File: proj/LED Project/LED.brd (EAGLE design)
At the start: 100 x 80 mm, 3 parts, among them U1 ATMEGA328P-AUR

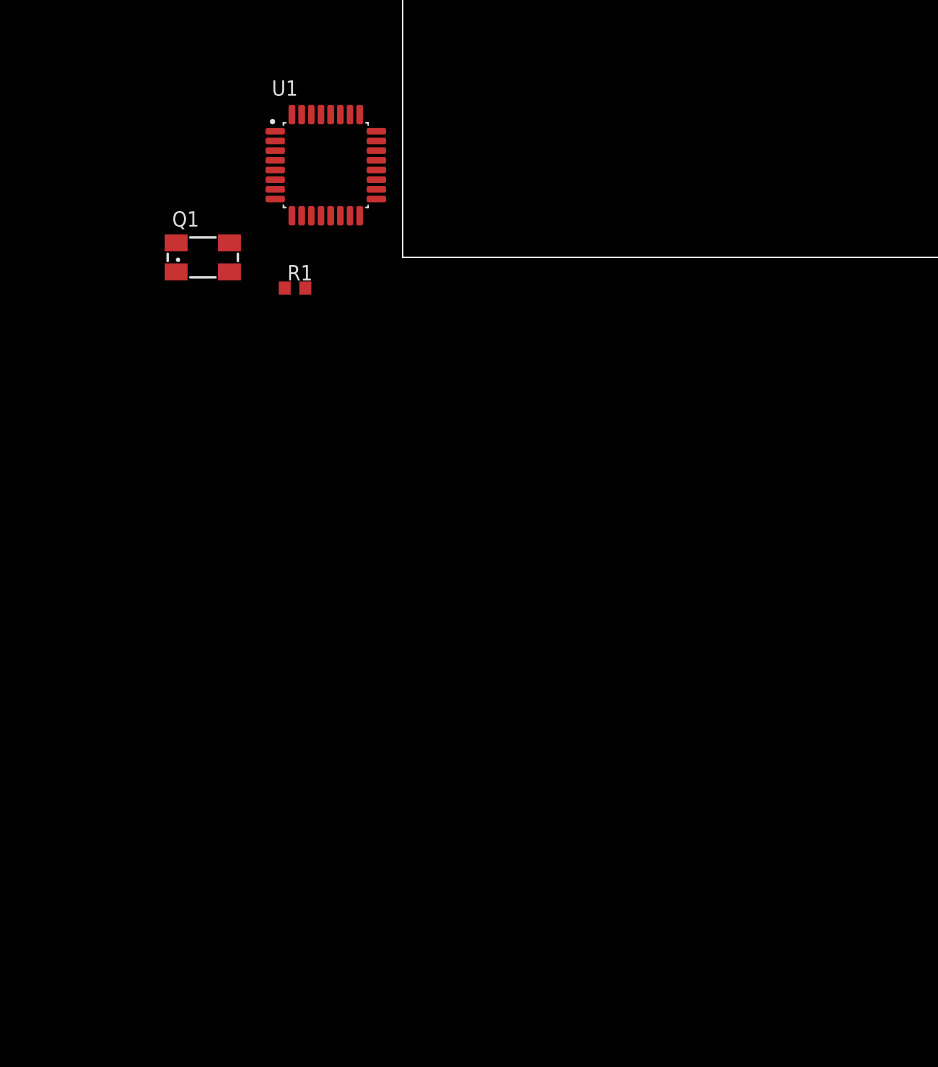
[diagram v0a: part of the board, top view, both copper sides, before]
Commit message: Working on the Schematic for a BareBones Arduino
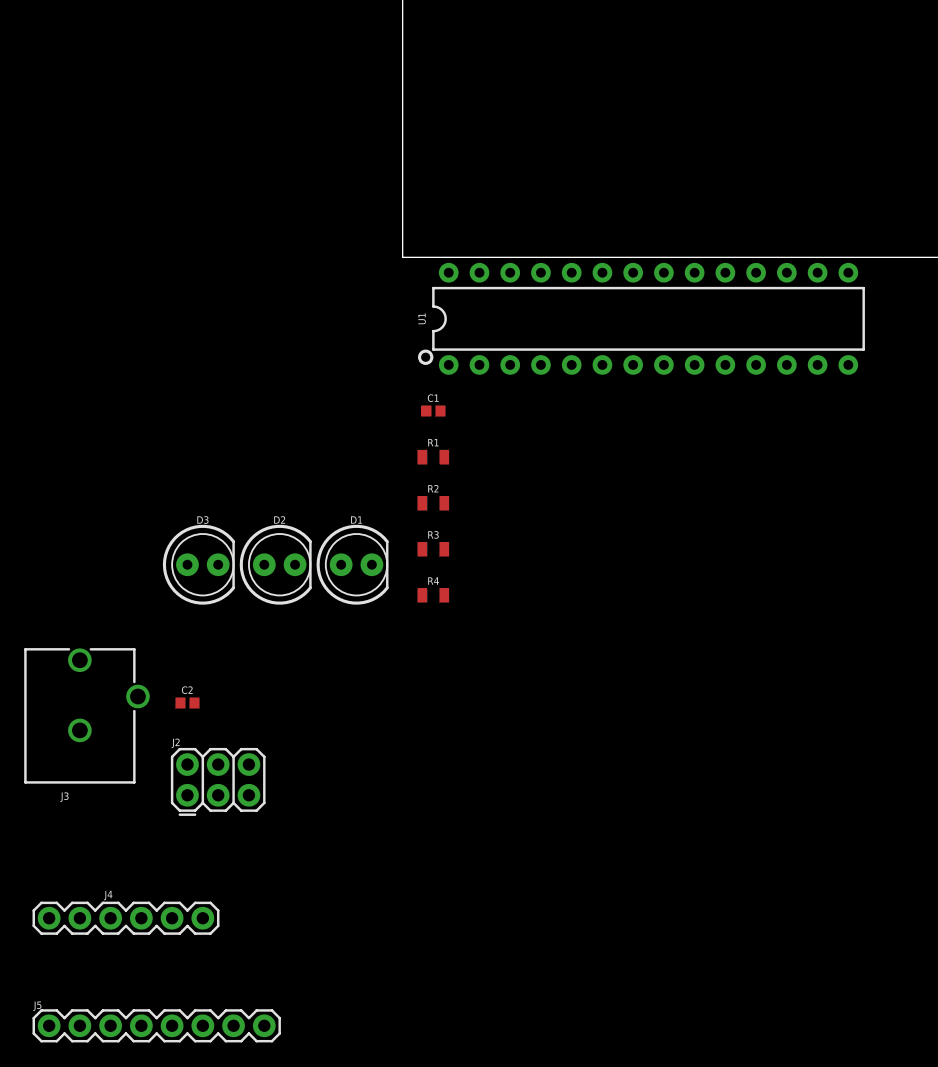
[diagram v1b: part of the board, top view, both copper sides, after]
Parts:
- removed Q1: (no value), crystal:CTS406
- added C1, C2: 0.1uF, SparkFun-Capacitors:0402
- added D1, D2, D3: (no value), SparkFun-LED:LED_5MM
- added J2: AVR_SPI_PROG_3X2PTH, SparkFun-Connectors:2X3
- added J3: POWER_JACKPTH_BREAD, SparkFun-Connectors:POWER_JACK_PTH_BREAD
- added J4: 6_PIN_SERIAL_CABLEPTH, SparkFun-Connectors:FTDI_BASIC
- added J5: (no value), SparkFun-Connectors:1X08
- added R2, R3, R4: 0.75, SparkFun-Resistors:0805
- R1: value 1M -> 0.75; device rcl:R0603 -> SparkFun-Resistors:0805
- U1: value ATMEGA328P-AUR -> 328P; device ATMEGA328P-AUR:QFP32P80_900X900X120L60X37N -> SparkFun-IC-Microcontroller:DIP28
- moved U1 29.5 mm to (20.3, -5.08)
- moved R1 18.1 mm to (2.54, -16.5)
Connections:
- removed net AREF: U1.20
- removed net AVCC: U1.18
- new net CTS: J4.CTS
- new net DTR: C1.1, J4.DTR
- new net MISO: J2.1, U1.18
- new net MOSI: J2.4, U1.17
- new net N$10: D3.A, U1.14
- new net N$11: D2.A, U1.15
- new net N$3: J5.3, U1.24
- new net N$4: J5.4, U1.25
- new net N$5: J5.5, U1.26
- new net N$6: J5.7, U1.28
- new net N$7: J5.6, U1.27
- new net N$8: D1.A, U1.16
- new net RESET: C1.2, J2.5, R4.1, U1.1, U1.20, U1.7
- new net RX: J4.RXI, U1.2
- new net SCK: J2.3, U1.19
- new net TX: J4.TXO, U1.3
- net GND: now also C2.1, D1.K, D2.K, J2.6, J3.GND, J3.GNDBREAK, J4.GND, J5.8, R1.1, R1.2, R2.1, R2.2, R3.1, U1.22, U1.8; no longer U1.21, U1.3, U1.5
- net N$1: now also J5.2, U1.23; no longer Q1.1, R1.2, U1.7
- net N$2: now also D3.K, R3.2; no longer Q1.3, R1.1, U1.8
- net VCC: now also C2.2, J2.2, J3.PWR, J4.VCC, J5.1, R4.2; no longer U1.4, U1.6

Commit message: Wired Board
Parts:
- moved J3 173.4 mm to (99.1, 72.4), turned to 90 degrees
- moved J5 154.1 mm to (33.0, 77.5), turned to 180 degrees
- moved C2 145.4 mm to (73.7, 76.2), turned to 270 degrees
- moved J2 136.3 mm to (45.7, 76.2), turned to 180 degrees
- moved J4 122.6 mm to (3.81, 63.5), turned to 90 degrees
- moved R4 122.0 mm to (78.7, 67.3)
- moved D1 117.7 mm to (63.5, 71.1)
- moved D2 115.5 mm to (63.5, 63.5)
- moved D3 113.2 mm to (63.5, 54.6)
- moved R1 112.1 mm to (72.4, 71.1), turned to 180 degrees
- moved R2 109.1 mm to (72.4, 63.5), turned to 180 degrees
- moved R3 105.3 mm to (72.4, 54.6), turned to 180 degrees
- moved U1 68.7 mm to (34.3, 62.2)
- moved C1 67.6 mm to (8.89, 54.6)
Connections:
- new net N$12: D2.K, R2.2
- new net N$9: D1.K, R1.2
- net GND: no longer D1.K, D2.K, R1.2, R2.2
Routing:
- net GND: track 0.00 -> 172.2 mm, vias 0 -> 1
- net RESET: track 0.00 -> 122.4 mm, vias 0 -> 7
- net VCC: track 0.00 -> 114.5 mm, vias 0 -> 1
- net TX: track 0.00 -> 39.6 mm
- net RX: track 0.00 -> 20.7 mm
- net N$8: track 0.00 -> 18.3 mm
- net N$10: track 0.00 -> 13.0 mm
- net N$11: track 0.00 -> 12.5 mm
- net MISO: track 0.00 -> 12.2 mm
- net SCK: track 0.00 -> 12.0 mm
- net N$7: track 0.00 -> 11.4 mm
- net N$6: track 0.00 -> 11.4 mm
- net N$5: track 0.00 -> 11.4 mm
- net N$4: track 0.00 -> 11.4 mm
- net N$3: track 0.00 -> 11.4 mm
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
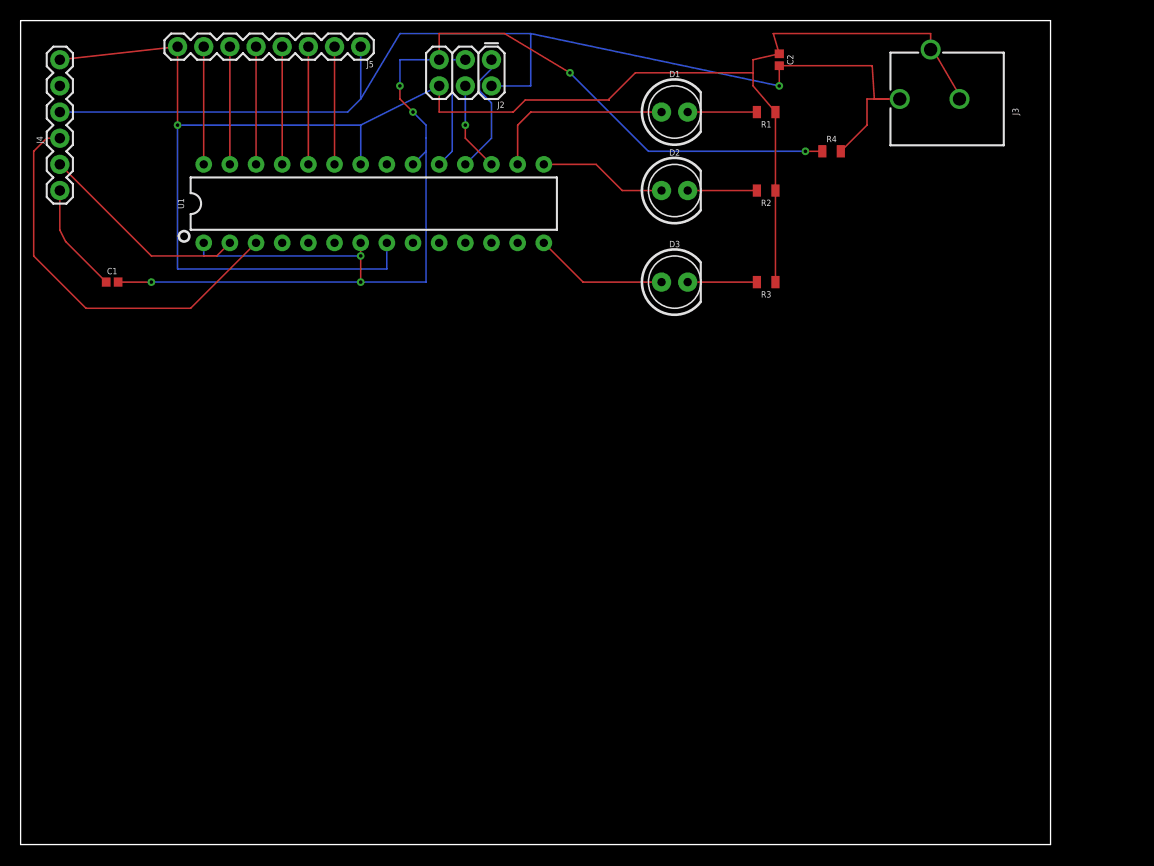
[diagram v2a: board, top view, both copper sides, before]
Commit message: Fixing Board Errors
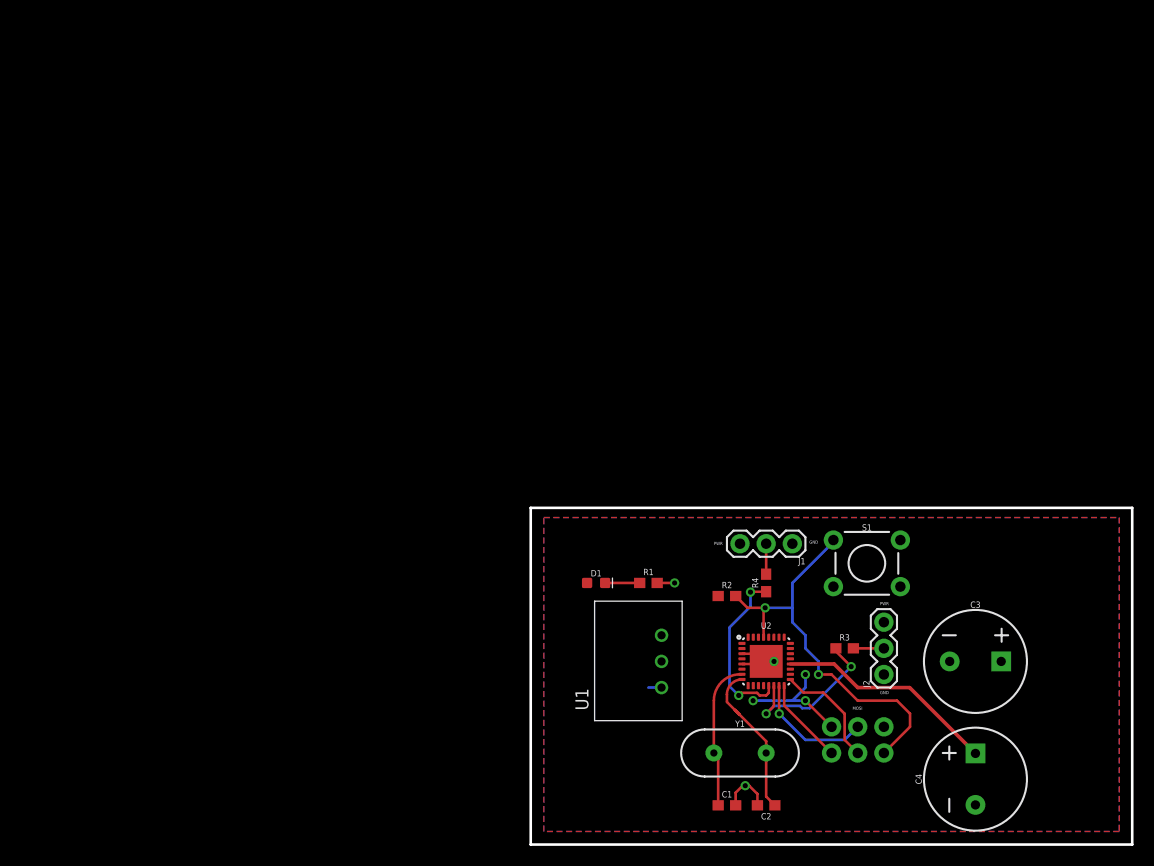
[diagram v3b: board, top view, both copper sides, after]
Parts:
- removed D2, D3: (no value), SparkFun-LED:LED_5MM
- removed J4: 6_PIN_SERIAL_CABLEPTH, SparkFun-Connectors:FTDI_BASIC
- removed J5: (no value), SparkFun-Connectors:1X08
- added C3: 1mF, SparkFun-Capacitors:CPOL-RADIAL-5MM-10MM
- added C4: 0.1 uF, SparkFun-Capacitors:CPOL-RADIAL-5MM-10MM
- added J1: (no value), SparkFun-Connectors:1X03
- added S1: MOMENTARY-SWITCH-SPST-PTH-6.0MM-KIT, SparkFun-Switches:TACTILE_SWITCH_PTH_6.0MM_KIT
- added U2: (no value), SparkFun-IC-Microcontroller:MLF32-PAD
- added Y1: 16MHz, SparkFun-Clocks:HC49US
- C1, C2: value 0.1uF -> 0.22uF; device SparkFun-Capacitors:0402 -> SparkFun-Capacitors:0603
- D1: value (none) -> GREEN; device SparkFun-LED:LED_5MM -> SparkFun-LED:LED-0603
- J2: value AVR_SPI_PROG_3X2PTH -> (none); device SparkFun-Connectors:2X3 -> SparkFun-Connectors:1X03
- J3: value POWER_JACKPTH_BREAD -> AVR_SPI_PROG_3X2NS; device SparkFun-Connectors:POWER_JACK_PTH_BREAD -> SparkFun-Connectors:2X3-NS
- R1: value 0.75 -> 200; device SparkFun-Resistors:0805 -> SparkFun-Resistors:0603
- R2: value 0.75 -> 10k; device SparkFun-Resistors:0805 -> SparkFun-Resistors:0603
- R3, R4: value 0.75 -> 400; device SparkFun-Resistors:0805 -> SparkFun-Resistors:0603
- U1: value 328P -> R-78E5.0-1.0; device SparkFun-IC-Microcontroller:DIP28 -> SparkFun-IC-Power:DC-DC_CONVERTER_78XX
- moved C1 78.4 mm to (68.6, 3.81)
- moved C2 72.4 mm to (72.4, 3.81), turned to 180 degrees
- moved J2 70.8 mm to (83.8, 16.5), turned to 90 degrees
- moved J3 64.7 mm to (81.3, 10.2), turned to 0 degrees
- moved U1 52.5 mm to (62.2, 17.8), turned to 90 degrees
- moved R1 47.1 mm to (61.0, 25.4), turned to 0 degrees
- moved D1 46.4 mm to (55.9, 25.4)
- moved R4 42.4 mm to (72.4, 25.4), turned to 90 degrees
- moved R2 39.6 mm to (68.6, 24.1), turned to 0 degrees
- moved R3 36.4 mm to (80.0, 19.1), turned to 0 degrees
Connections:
- removed net CTS: J4.CTS
- removed net DTR: C1.1, J4.DTR
- removed net N$1: J5.2, U1.23
- removed net N$11: D2.A, U1.15
- removed net N$12: D2.K, R2.2
- removed net N$2: D3.K, R3.2
- removed net N$3: J5.3, U1.24
- removed net N$4: J5.4, U1.25
- removed net N$5: J5.5, U1.26
- removed net N$6: J5.7, U1.28
- removed net N$7: J5.6, U1.27
- removed net N$8: D1.A, U1.16
- removed net N$9: D1.K, R1.2
- removed net RESET: C1.2, J2.5, R4.1, U1.1, U1.20, U1.7
- new net 9V: U1.VIN
- new net DATA1: J1.2, R4.2
- new net DATA2: J2.2, R3.2
- new net NP1: R4.1, U2.13
- new net NP2: R3.1, U2.14
- new net RST: J3.5, R2.2, S1.1, U2.29
- new net VCC1: C4.+, U2.20
- new net XTAL1: C1.1, U2.7, Y1.1
- new net XTAL2: C2.1, U2.8, Y1.2
- net GND: now also C1.2, C2.2, C3.-, C4.-, J1.1, J2.1, J3.6, R1.2, S1.3, U1.GND, U2.3, U2.5, U2.PAD; no longer C2.1, J2.6, J3.GND, J3.GNDBREAK, J4.GND, J5.8, R1.1, R2.1, R3.1, U1.22, U1.8
- net MISO: now also J3.1, U2.16; no longer J2.1, U1.18
- net MOSI: now also J3.4, U2.15; no longer J2.4, U1.17
- net N$10: now also D1.C, R1.1; no longer D3.A, U1.14
- net RX: now also U2.30; no longer J4.RXI, U1.2
- net SCK: now also J3.3, U2.17; no longer J2.3, U1.19
- net TX: now also U2.31; no longer J4.TXO, U1.3
- net VCC: now also C3.+, D1.A, J1.3, J2.3, J3.2, R2.1, U1.VOUT, U2.18, U2.4, U2.6; no longer C2.2, J2.2, J3.PWR, J4.VCC, J5.1, R4.2
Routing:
- net GND: track 172.2 -> 12.6 mm, vias 1 -> 3
- net RESET: track 122.4 -> 0.00 mm, vias 7 -> 0
- net VCC: track 114.5 -> 11.7 mm, vias 1 -> 3
- net RST: track 0.00 -> 40.0 mm, vias 0 -> 2
- net TX: track 39.6 -> 0.00 mm
- net VCC1: track 0.00 -> 21.6 mm
- net RX: track 20.7 -> 0.00 mm
- net N$8: track 18.3 -> 0.00 mm
- net NP1: track 0.00 -> 16.7 mm, vias 0 -> 2
- net XTAL2: track 0.00 -> 16.0 mm
- net NP2: track 0.00 -> 15.8 mm, vias 0 -> 2
- net XTAL1: track 0.00 -> 14.1 mm
- net N$11: track 12.5 -> 0.00 mm
- net N$7: track 11.4 -> 0.00 mm
- net N$6: track 11.4 -> 0.00 mm
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- added copper zone on layer 16, net GND
- added copper zone on layer 1, net VCC
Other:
- board size 100 x 80 mm -> 58.4 x 32.7 mm
- board text added: "GND"
- board text added: "MOSI"
- board text added: "PWR"

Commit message: fixing schematic
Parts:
- added C5: 10uF, SparkFun-Capacitors:CPOL-RADIAL-5MM-10MM
- added C6: 10uF, rcl:C0805
- U2: value (none) -> ATMEGA328P_MLF
- moved U1 37.0 mm to (99.1, 21.6), turned to 180 degrees
- moved C2 29.6 mm to (57.1, 29.2), turned to 90 degrees
- moved C1 26.2 mm to (62.2, 29.2), turned to 90 degrees
- moved J1 21.6 mm to (59.7, 14.0), turned to 270 degrees
- moved R1 20.5 mm to (58.4, 5.08)
- moved D1 20.4 mm to (54.6, 5.08)
- moved C4 19.7 mm to (87.6, 25.4), turned to 180 degrees
- moved Y1 18.3 mm to (59.7, 24.1), turned to 180 degrees
- moved R4 16.6 mm to (63.5, 11.4), turned to 180 degrees
- moved J2 16.2 mm to (72.4, 5.08), turned to 180 degrees
- moved R3 14.4 mm to (69.8, 8.89), turned to 270 degrees
- moved S1 6.86 mm to (75.3, 27.3), turned to 180 degrees
- moved C3 6.35 mm to (87.6, 14.0)
- moved J3 4.02 mm to (80.0, 6.35)
- moved R2 1.27 mm to (68.6, 22.9)
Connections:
- net VCC1 renamed N$1
- new net N$2: C3.+
- new net N$5: C6.1, U1.VOUT
- net 9V: now also C5.+
- net GND: now also C5.-, C6.2, U2.21
- net VCC: no longer C3.+, U1.VOUT
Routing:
- net N$5: track 0.00 -> 17.2 mm
- net 9V: track 1.27 -> 15.7 mm
- net VCC: track 11.7 -> 0.00 mm, vias 3 -> 0
- net NP2: track 15.8 -> 7.05 mm, vias 2 -> 0
- net N$1: track 21.6 -> 13.9 mm
- net NP1: track 16.7 -> 10.8 mm, vias 2 -> 0
- net XTAL2: track 16.0 -> 21.2 mm
- net RST: track 40.0 -> 35.1 mm, vias 2 -> 1
- net MISO: track 8.45 -> 11.7 mm
- net SCK: track 11.0 -> 14.3 mm, vias 0 -> 1
- net GND: track 12.6 -> 14.6 mm, vias 3 -> 11
- net XTAL1: track 14.1 -> 15.7 mm
- net N$10: track 3.35 -> 2.08 mm

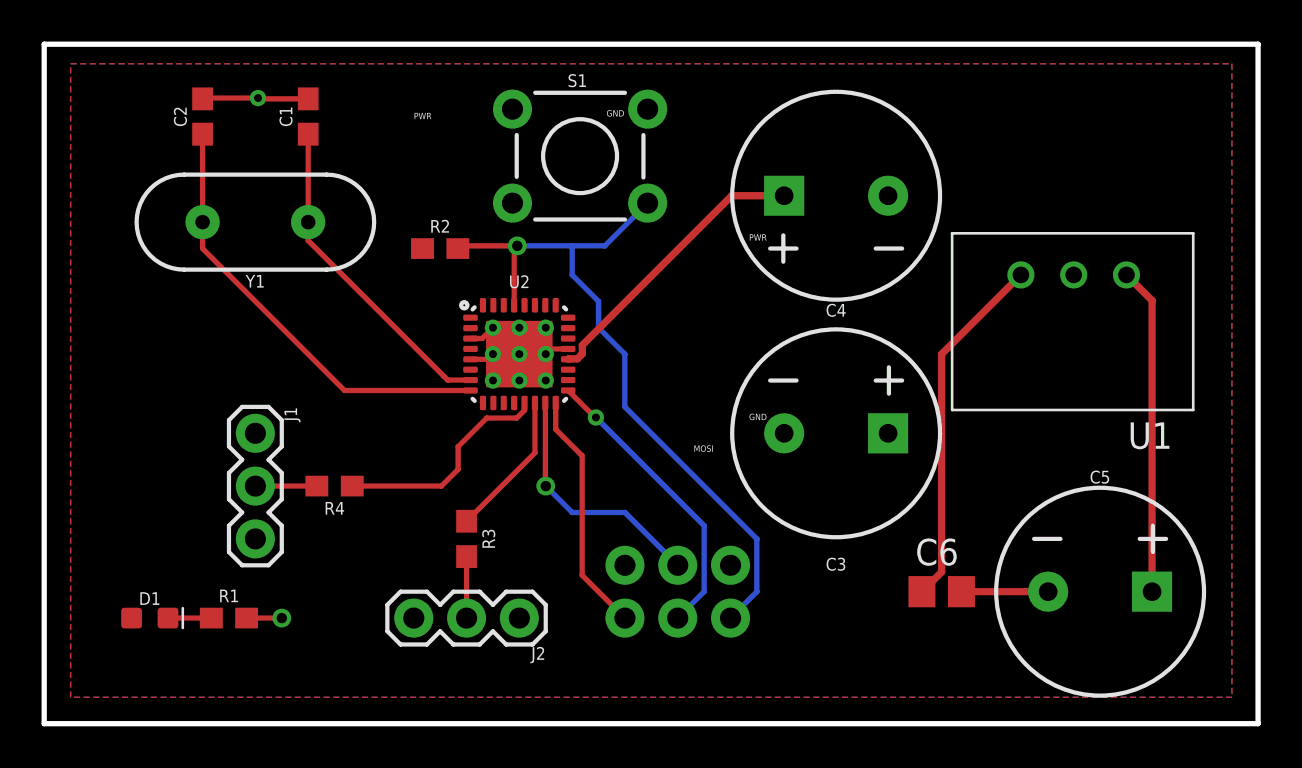
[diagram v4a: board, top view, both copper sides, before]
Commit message: Added IGVC lbr so I have them and a fuse
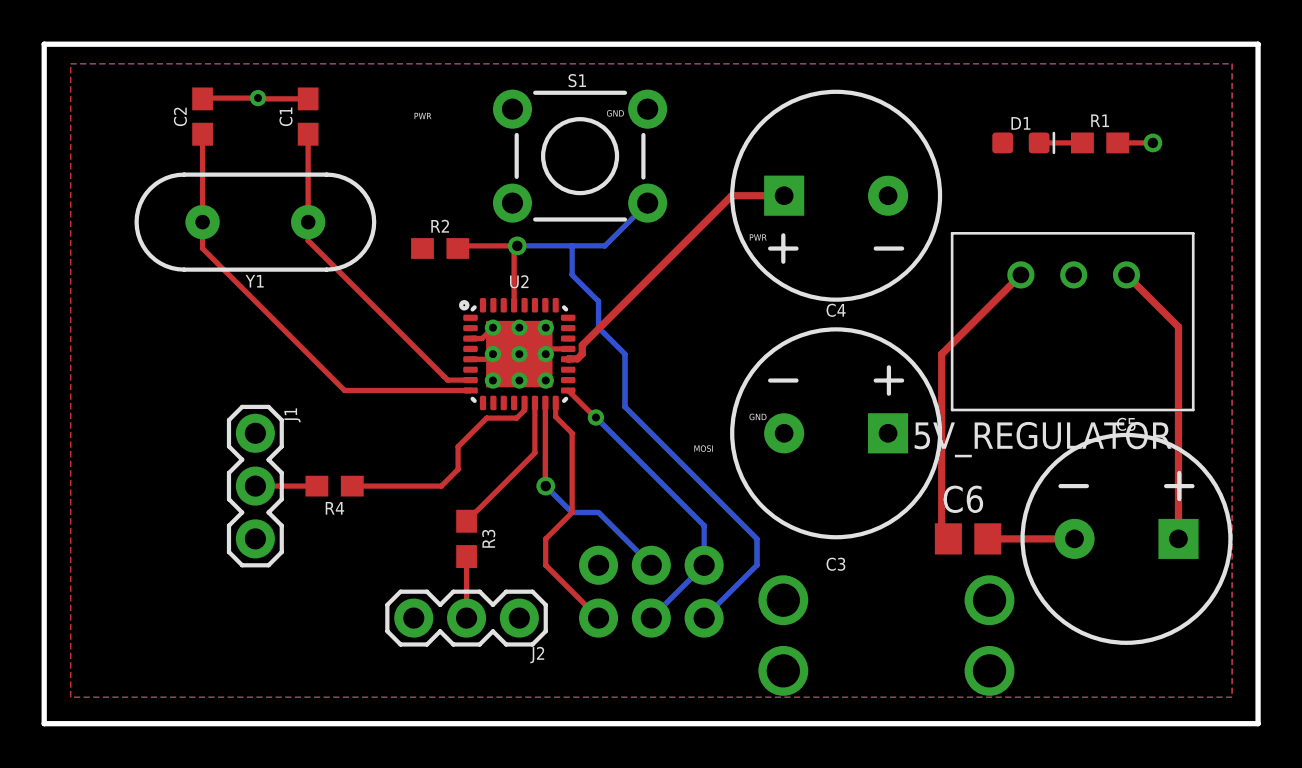
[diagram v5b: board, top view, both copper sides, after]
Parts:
- added FUSE: 3.6A, IGVC-Misc:FUSE_HOLDER
- moved D1 47.7 mm to (96.5, 27.9)
- moved R1 47.7 mm to (100.3, 27.9)
- moved C6 2.84 mm to (94.0, 8.89)
- moved C5 2.84 mm to (101.6, 8.89)
- moved J3 1.27 mm to (78.7, 6.35)
- renumbered U1 to 5V_REGULATOR
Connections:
- removed net N$2: C3.+
- net N$5: now also FUSE.P$3, FUSE.P$4
- net VCC: now also C3.+, FUSE.P$1, FUSE.P$2
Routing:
- net N$5: track 17.2 -> 14.4 mm
- net 9V: track 15.7 -> 13.7 mm
- net MOSI: track 11.9 -> 10.7 mm
- net MISO: track 11.7 -> 12.3 mm
- net SCK: track 14.3 -> 14.8 mm
- net RST: track 35.1 -> 35.6 mm
